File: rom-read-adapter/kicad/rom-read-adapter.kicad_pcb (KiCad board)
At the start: 2 copper layers, 100 x 100 mm, 27 parts

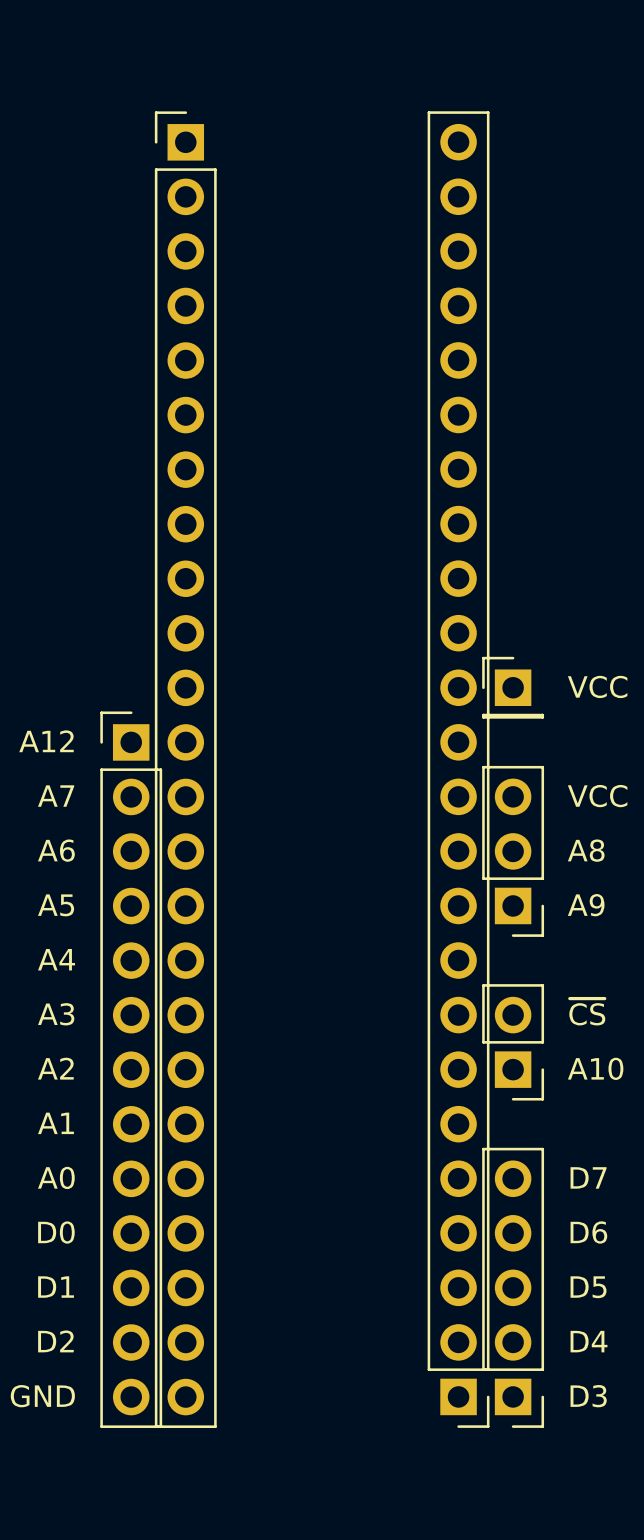
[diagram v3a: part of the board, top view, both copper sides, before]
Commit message: WIP rom-read-adapter pcb: ROM connection area pin numbering
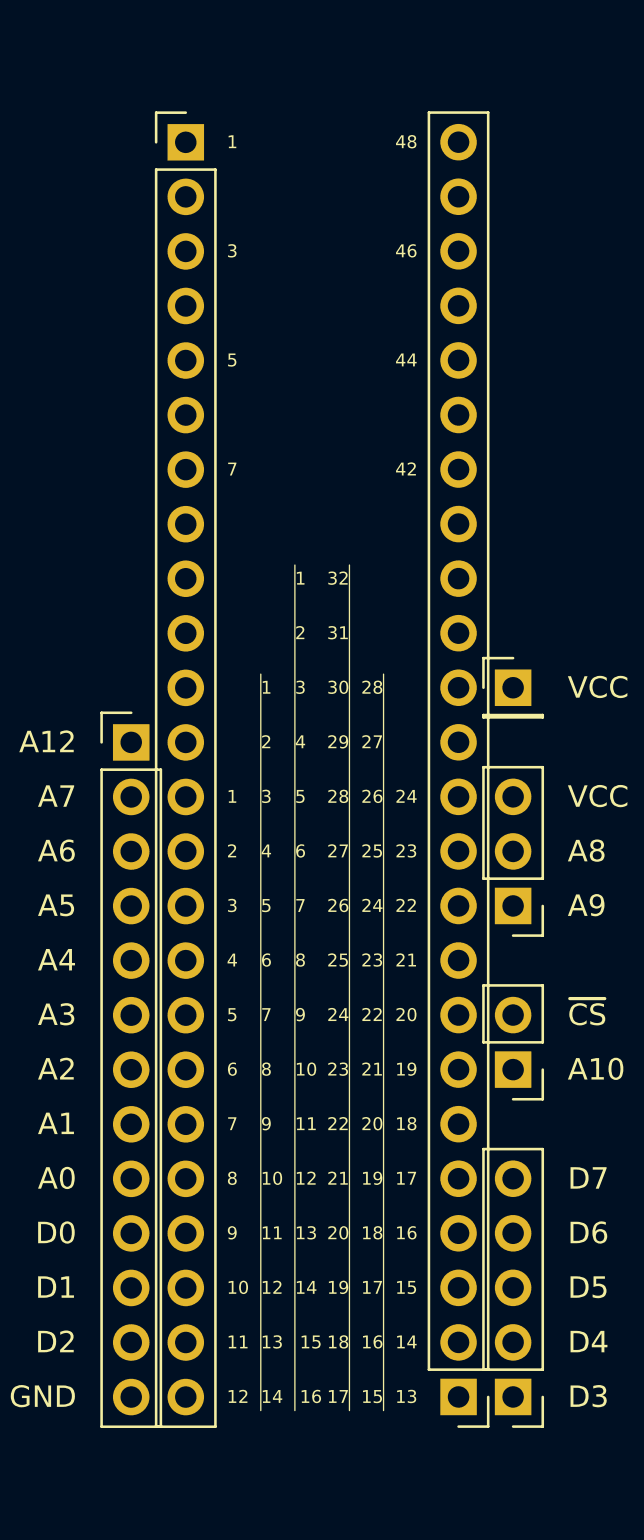
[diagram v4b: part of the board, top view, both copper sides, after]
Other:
- board text added: "20"
- board text added: "21"
- board text added: "22"
- board text added: "23"
- board text added: "24"
- board text added: "25"
- board text added: "26"
- board text added: "27"
- board text added: "28"
- board text added: "29"
- board text added: "30"
- board text added: "31"
- board text added: "32"
- board text added: "42"
- board text added: "44"
- board text added: "46"
- board text added: "48"

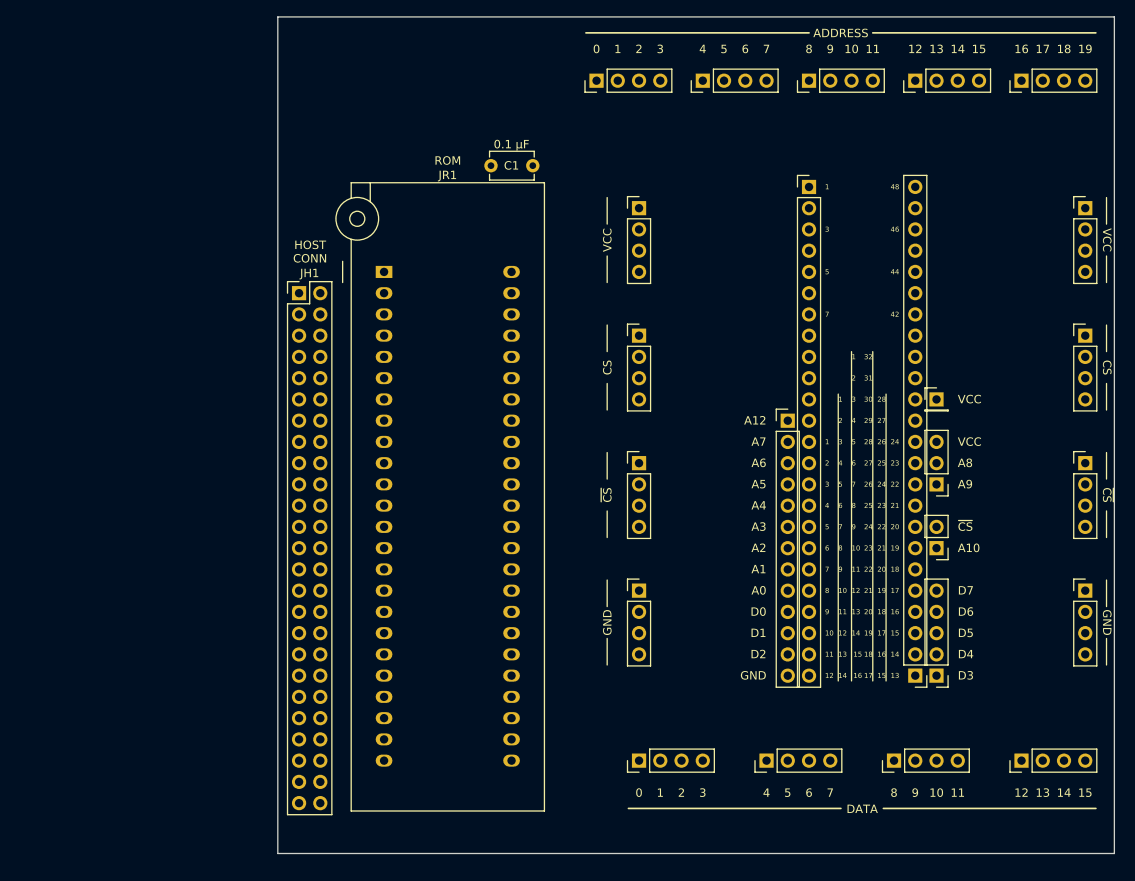
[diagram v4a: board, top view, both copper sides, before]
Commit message: WIP rom-read-adapter pcb: Route VCC, GND, CS and Non CS
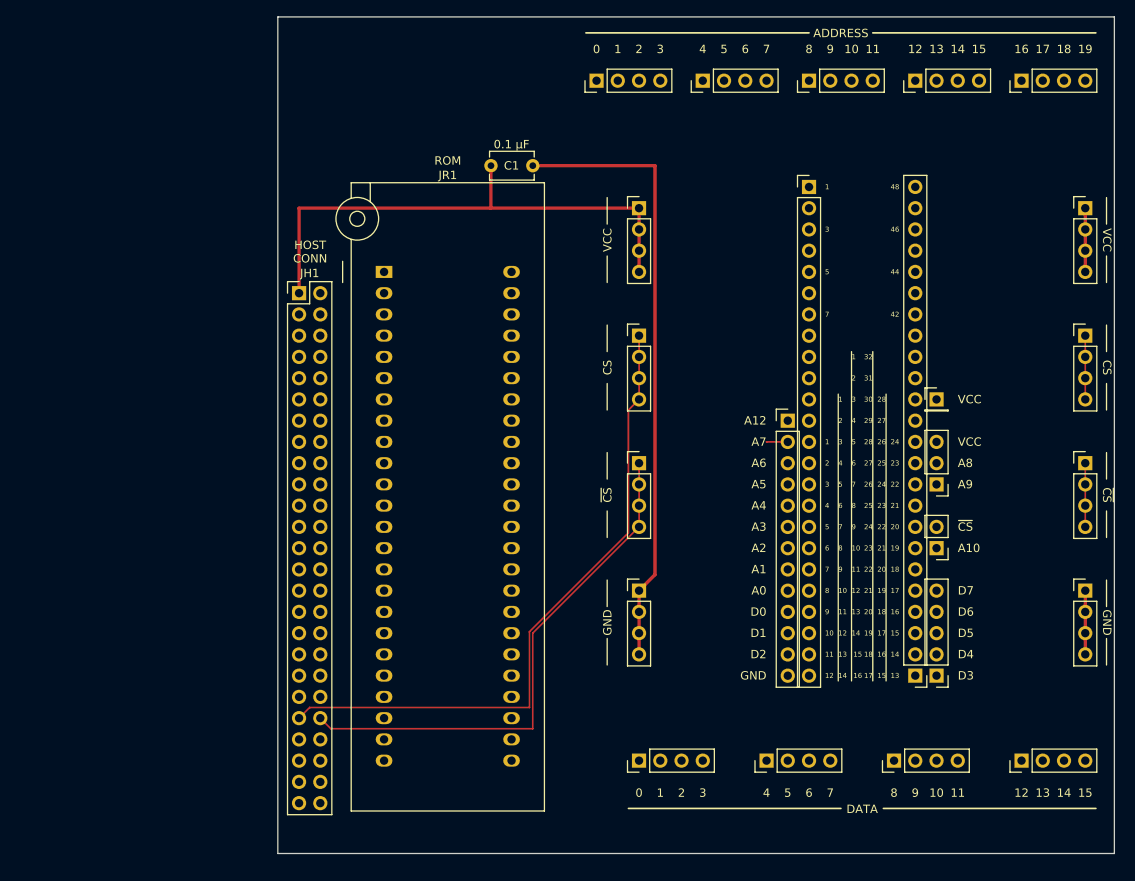
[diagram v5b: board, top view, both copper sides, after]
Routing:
- net CS: track 0.00 -> 85.6 mm
- net GND: track 0.00 -> 81.4 mm
- net VCC: track 0.00 -> 71.2 mm
- net ~{CS}: track 0.00 -> 70.6 mm
- net A7: track 0.00 -> 2.54 mm
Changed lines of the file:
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@@
 		)
+	)
+	(segment
+		(start 198.12 119.38)
+		(end 198.12 127)
+		(width 0.4)
+		(layer "F.Cu")
+		(net 1)
+	)
+	(segment
+		(start 146.685 117.475)
+		(end 146.685 68.58)
+		(width 0.4)
+		(layer "F.Cu")
+		(net 1)
+	)
+	(segment
+		(start 146.685 68.58)
+		(end 132.08 68.58)
+		(width 0.4)
+		(layer "F.Cu")
+		(net 1)
+	)
+	(segment
+		(start 144.78 119.38)
+		(end 146.685 117.475)
+		(width 0.4)
+		(layer "F.Cu")
+		(net 1)
+	)
+	(segment
+		(start 144.78 119.38)
+		(end 144.78 127)
+		(width 0.4)
+		(layer "F.Cu")
+		(net 1)
+	)
+	(segment
+		(start 104.14 73.66)
+		(end 104.14 83.82)
+		(width 0.4)
+		(layer "F.Cu")
+		(net 2)
+	)
+	(segment
+		(start 127 73.66)
+		(end 104.14 73.66)
+		(width 0.4)
+		(layer "F.Cu")
+		(net 2)
+	)
+	(segment
+		(start 144.78 73.66)
+		(end 144.78 81.28)
+		(width 0.4)
+		(layer "F.Cu")
+		(net 2)
+	)
+	(segment
+		(start 198.12 73.66)
+		(end 198.12 81.28)
+		(width 0.4)
+		(layer "F.Cu")
+		(net 2)
+	)
+	(segment
+		(start 127.08 73.58)
+		(end 127 73.66)
+		(width 0.2)
+		(layer "F.Cu")
+		(net 2)
+	)
+	(segment
+		(start 144.78 73.66)
+		(end 127 73.66)
+		(width 0.4)
+		(layer "F.Cu")
+		(net 2)
+	)
+	(segment
+		(start 127.08 68.58)
+		(end 127.08 73.58)
+		(width 0.4)
+		(layer "F.Cu")
+		(net 2)
+	)
+	(segment
+		(start 131.679 124.2939)
+		(end 131.679 133.35)
+		(width 0.2)
+		(layer "F.Cu")
+		(net 19)
+	)
+	(segment
+		(start 143.51 97.79)
+		(end 143.51 112.4629)
+		(width 0.2)
+		(layer "F.Cu")
+		(net 19)
+	)
+	(segment
+		(start 144.78 88.9)
+		(end 144.78 96.52)
+		(width 0.2)
+		(layer "F.Cu")
+		(net 19)
+	)
+	(segment
+		(start 105.41 133.35)
+		(end 104.14 134.62)
+		(width 0.2)
+		(layer "F.Cu")
+		(net 19)
+	)
+	(segment
+		(start 144.78 96.52)
+		(end 143.51 97.79)
+		(width 0.2)
+		(layer "F.Cu")
+		(net 19)
+	)
+	(segment
+		(start 143.51 112.4629)
+		(end 131.679 124.2939)
+		(width 0.2)
+		(layer "F.Cu")
+		(net 19)
+	)
+	(segment
+		(start 198.12 88.9)
+		(end 198.12 96.52)
+		(width 0.2)
+		(layer "F.Cu")
+		(net 19)
+	)
+	(segment
+		(start 131.679 133.35)
+		(end 105.41 133.35)
+		(width 0.2)
+		(layer "F.Cu")
+		(net 19)
+	)
+	(segment
+		(start 162.56 101.605)
+		(end 160.025 101.605)
+		(width 0.2)
+		(layer "F.Cu")
+		(net 22)
+	)
+	(segment
+		(start 160.025 101.605)
+		(end 160.02 101.6)
+		(width 0.2)
+		(layer "F.Cu")
+		(net 22)
+	)
+	(segment
+		(start 198.12 104.14)
+		(end 198.12 111.76)
+		(width 0.2)
+		(layer "F.Cu")
+		(net 36)
+	)
+	(segment
+		(start 107.95 135.89)
+		(end 132.08 135.89)
+		(width 0.2)
+		(layer "F.Cu")
+		(net 36)
+	)
+	(segment
+		(start 132.08 135.89)
+		(end 132.08 124.46)
+		(width 0.2)
+		(layer "F.Cu")
+		(net 36)
+	)
+	(segment
+		(start 132.08 124.46)
+		(end 144.78 111.76)
+		(width 0.2)
+		(layer "F.Cu")
+		(net 36)
+	)
+	(segment
+		(start 106.68 134.62)
+		(end 107.95 135.89)
+		(width 0.2)
+		(layer "F.Cu")
+		(net 36)
+	)
+	(segment
+		(start 144.78 104.14)
+		(end 144.78 111.76)
+		(width 0.2)
+		(layer "F.Cu")
+		(net 36)
+	)
+	(segment
+		(start 162.56 121.925)
+		(end 162.56 121.92)
+		(width 0.2)
+		(layer "F.Cu")
+		(net 38)
 	)
 	(embedded_fonts no)

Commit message: WIP rom-read-adapter pcb: New routing approach
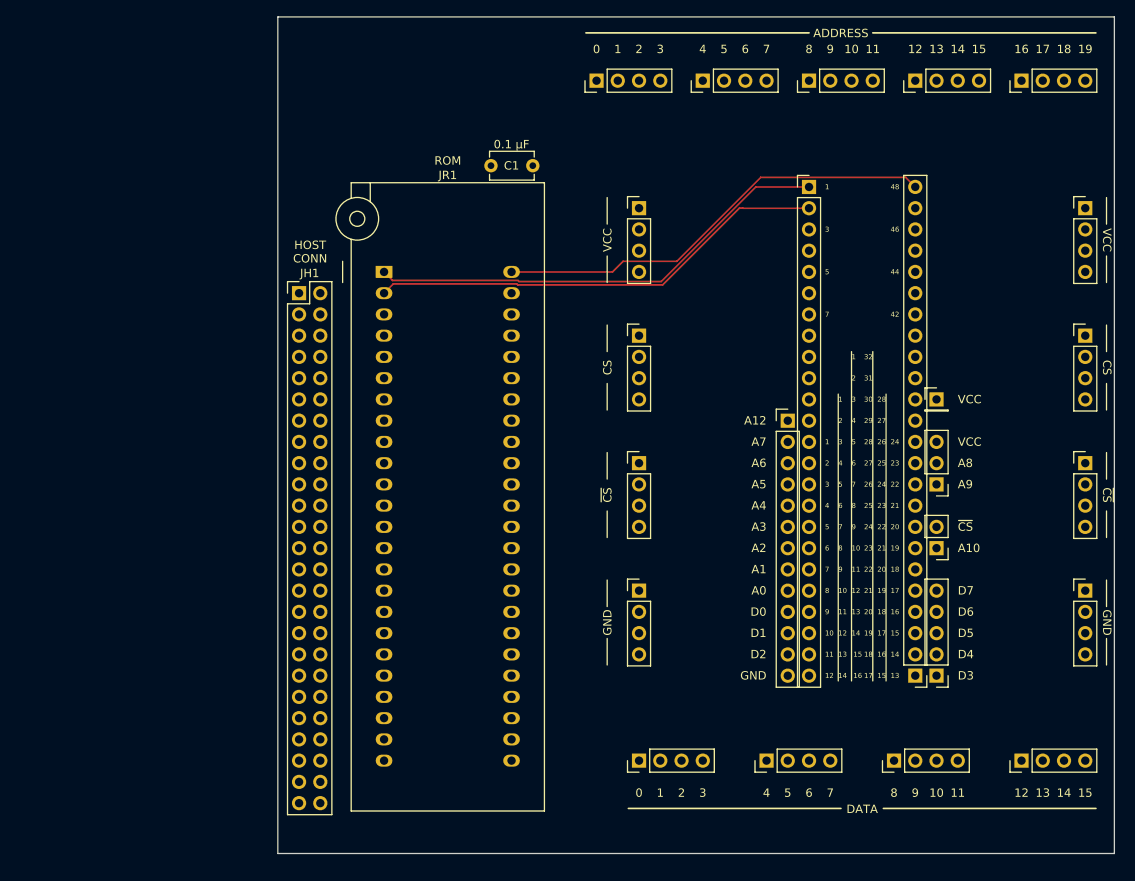
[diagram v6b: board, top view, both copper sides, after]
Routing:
- net CS: track 85.6 -> 0.00 mm
- net GND: track 81.4 -> 0.00 mm
- net VCC: track 71.2 -> 0.00 mm
- net ~{CS}: track 70.6 -> 0.00 mm
- net Net-(JR1-Pin_1): track 0.00 -> 56.0 mm
- net Net-(JR1-Pin_2): track 0.00 -> 55.1 mm
- net Net-(JR1-Pin_48): track 0.00 -> 53.4 mm
- net A7: track 2.54 -> 0.00 mm
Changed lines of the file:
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@@
-	)
-	(segment
-		(start 198.12 119.38)
-		(end 198.12 127)
-		(width 0.4)
-		(layer "F.Cu")
-		(net 1)
-	)
-	(segment
-		(start 146.685 117.475)
-		(end 146.685 68.58)
-		(width 0.4)
-		(layer "F.Cu")
-		(net 1)
-	)
-	(segment
-		(start 146.685 68.58)
-		(end 132.08 68.58)
-		(width 0.4)
-		(layer "F.Cu")
-		(net 1)
-	)
-	(segment
-		(start 144.78 119.38)
-		(end 146.685 117.475)
-		(width 0.4)
-		(layer "F.Cu")
-		(net 1)
-	)
-	(segment
-		(start 144.78 119.38)
-		(end 144.78 127)
-		(width 0.4)
-		(layer "F.Cu")
-		(net 1)
-	)
-	(segment
-		(start 104.14 73.66)
-		(end 104.14 83.82)
-		(width 0.4)
-		(layer "F.Cu")
-		(net 2)
-	)
-	(segment
-		(start 127 73.66)
-		(end 104.14 73.66)
-		(width 0.4)
-		(layer "F.Cu")
-		(net 2)
-	)
-	(segment
-		(start 144.78 73.66)
-		(end 144.78 81.28)
-		(width 0.4)
-		(layer "F.Cu")
-		(net 2)
-	)
-	(segment
-		(start 198.12 73.66)
-		(end 198.12 81.28)
-		(width 0.4)
-		(layer "F.Cu")
-		(net 2)
-	)
-	(segment
-		(start 127.08 73.58)
-		(end 127 73.66)
-		(width 0.2)
-		(layer "F.Cu")
-		(net 2)
-	)
-	(segment
-		(start 144.78 73.66)
-		(end 127 73.66)
-		(width 0.4)
-		(layer "F.Cu")
-		(net 2)
-	)
-	(segment
-		(start 127.08 68.58)
-		(end 127.08 73.58)
-		(width 0.4)
-		(layer "F.Cu")
-		(net 2)
-	)
-	(segment
-		(start 131.679 124.2939)
-		(end 131.679 133.35)
-		(width 0.2)
-		(layer "F.Cu")
-		(net 19)
-	)
-	(segment
-		(start 143.51 97.79)
-		(end 143.51 112.4629)
-		(width 0.2)
-		(layer "F.Cu")
-		(net 19)
-	)
-	(segment
-		(start 144.78 88.9)
-		(end 144.78 96.52)
-		(width 0.2)
-		(layer "F.Cu")
-		(net 19)
-	)
-	(segment
-		(start 105.41 133.35)
-		(end 104.14 134.62)
-		(width 0.2)
-		(layer "F.Cu")
-		(net 19)
-	)
-	(segment
-		(start 144.78 96.52)
-		(end 143.51 97.79)
-		(width 0.2)
-		(layer "F.Cu")
-		(net 19)
-	)
-	(segment
-		(start 143.51 112.4629)
-		(end 131.679 124.2939)
-		(width 0.2)
-		(layer "F.Cu")
-		(net 19)
-	)
-	(segment
-		(start 198.12 88.9)
-		(end 198.12 96.52)
-		(width 0.2)
-		(layer "F.Cu")
-		(net 19)
-	)
-	(segment
-		(start 131.679 133.35)
-		(end 105.41 133.35)
-		(width 0.2)
-		(layer "F.Cu")
-		(net 19)
-	)
-	(segment
-		(start 162.56 101.605)
-		(end 160.025 101.605)
-		(width 0.2)
-		(layer "F.Cu")
-		(net 22)
-	)
-	(segment
-		(start 160.025 101.605)
-		(end 160.02 101.6)
-		(width 0.2)
-		(layer "F.Cu")
-		(net 22)
-	)
-	(segment
-		(start 198.12 104.14)
-		(end 198.12 111.76)
-		(width 0.2)
-		(layer "F.Cu")
-		(net 36)
-	)
-	(segment
-		(start 107.95 135.89)
-		(end 132.08 135.89)
-		(width 0.2)
-		(layer "F.Cu")
-		(net 36)
-	)
-	(segment
-		(start 132.08 135.89)
-		(end 132.08 124.46)
-		(width 0.2)
-		(layer "F.Cu")
-		(net 36)
-	)
-	(segment
-		(start 132.08 124.46)
-		(end 144.78 111.76)
-		(width 0.2)
-		(layer "F.Cu")
-		(net 36)
-	)
-	(segment
-		(start 106.68 134.62)
-		(end 107.95 135.89)
-		(width 0.2)
-		(layer "F.Cu")
-		(net 36)
-	)
-	(segment
-		(start 144.78 104.14)
-		(end 144.78 111.76)
-		(width 0.2)
-		(layer "F.Cu")
-		(net 36)
 	)
 	(segment
@@
 		(net 38)
 	)
+	(segment
+		(start 147.439 82.431)
+		(end 130.442012 82.431)
+		(width 0.2)
+		(layer "F.Cu")
+		(net 55)
+	)
+	(segment
+		(start 165.1 71.125)
+		(end 158.745 71.125)
+		(width 0.2)
+		(layer "F.Cu")
+		(net 55)
+	)
+	(segment
+		(start 130.312012 82.301)
+		(end 115.321 82.301)
+		(width 0.2)
+		(layer "F.Cu")
+		(net 55)
+	)
+	(segment
+		(start 130.442012 82.431)
+		(end 130.312012 82.301)
+		(width 0.2)
+		(layer "F.Cu")
+		(net 55)
+	)
+	(segment
+		(start 115.321 82.301)
+		(end 114.3 81.28)
+		(width 0.2)
+		(layer "F.Cu")
+		(net 55)
+	)
+	(segment
+		(start 158.745 71.125)
+		(end 147.439 82.431)
+		(width 0.2)
+		(layer "F.Cu")
+		(net 55)
+	)
+	(segment
+		(start 159.3289 69.974)
+		(end 176.654 69.974)
+		(width 0.2)
+		(layer "F.Cu")
+		(net 62)
+	)
+	(segment
+		(start 141.605 81.28)
+		(end 142.875 80.01)
+		(width 0.2)
+		(layer "F.Cu")
+		(net 62)
+	)
+	(segment
+		(start 149.2929 80.01)
+		(end 159.3289 69.974)
+		(width 0.2)
+		(layer "F.Cu")
+		(net 62)
+	)
+	(segment
+		(start 129.54 81.28)
+		(end 141.605 81.28)
+		(width 0.2)
+		(layer "F.Cu")
+		(net 62)
+	)
+	(segment
+		(start 142.875 80.01)
+		(end 149.2929 80.01)
+		(width 0.2)
+		(layer "F.Cu")
+		(net 62)
+	)
+	(segment
+		(start 176.654 69.974)
+		(end 177.8 71.12)
+		(width 0.2)
+		(layer "F.Cu")
+		(net 62)
+	)
+	(segment
+		(start 130.145912 82.702)
+		(end 130.275912 82.832)
+		(width 0.2)
+		(layer "F.Cu")
+		(net 67)
+	)
+	(segment
+		(start 156.7771 73.66)
+		(end 157.1625 73.66)
+		(width 0.2)
+		(layer "F.Cu")
+		(net 67)
+	)
+	(segment
+		(start 147.6051 82.832)
+		(end 156.7771 73.66)
+		(width 0.2)
+		(layer "F.Cu")
+		(net 67)
+	)
+	(segment
+		(start 114.3 83.82)
+		(end 115.418 82.702)
+		(width 0.2)
+		(layer "F.Cu")
+		(net 67)
+	)
+	(segment
+		(start 130.275912 82.832)
+		(end 147.6051 82.832)
+		(width 0.2)
+		(layer "F.Cu")
+		(net 67)
+	)
+	(segment
+		(start 157.1675 73.665)
+		(end 165.1 73.665)
+		(width 0.2)
+		(layer "F.Cu")
+		(net 67)
+	)
+	(segment
+		(start 157.1625 73.66)
+		(end 157.1675 73.665)
+		(width 0.2)
+		(layer "F.Cu")
+		(net 67)
+	)
+	(segment
+		(start 115.418 82.702)
+		(end 130.145912 82.702)
+		(width 0.2)
+		(layer "F.Cu")
+		(net 67)
+	)
 	(embedded_fonts no)
